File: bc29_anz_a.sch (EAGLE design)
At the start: 10 parts, among them IC2 MM74C945N, J1 2520-5

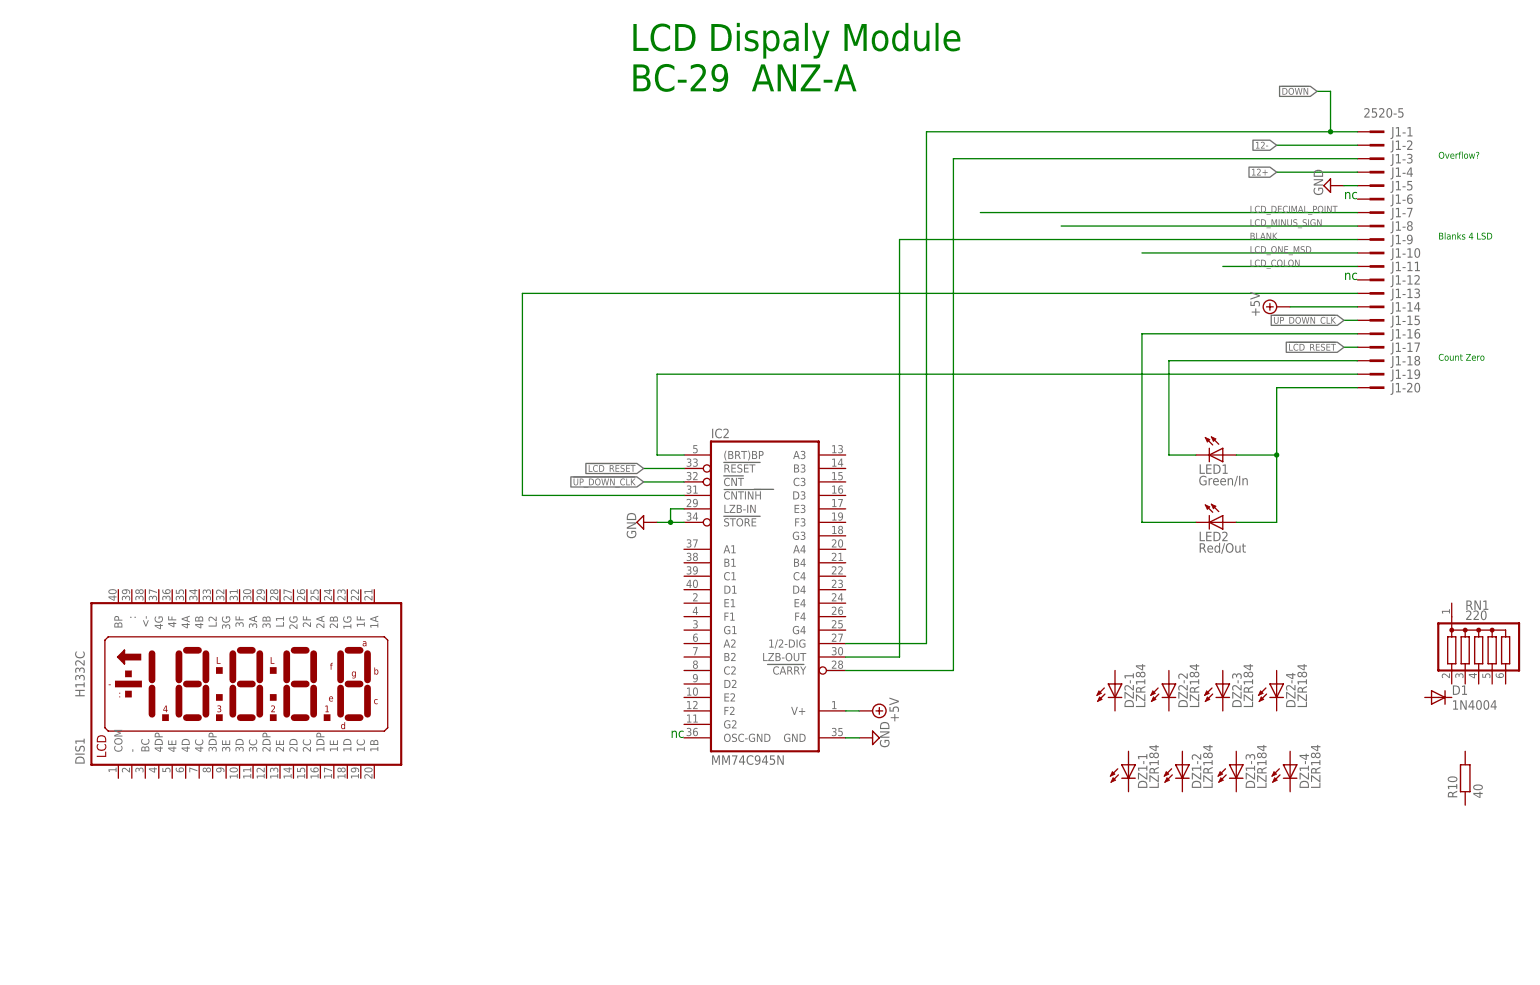
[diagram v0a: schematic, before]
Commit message: Incorperate display module knowldge
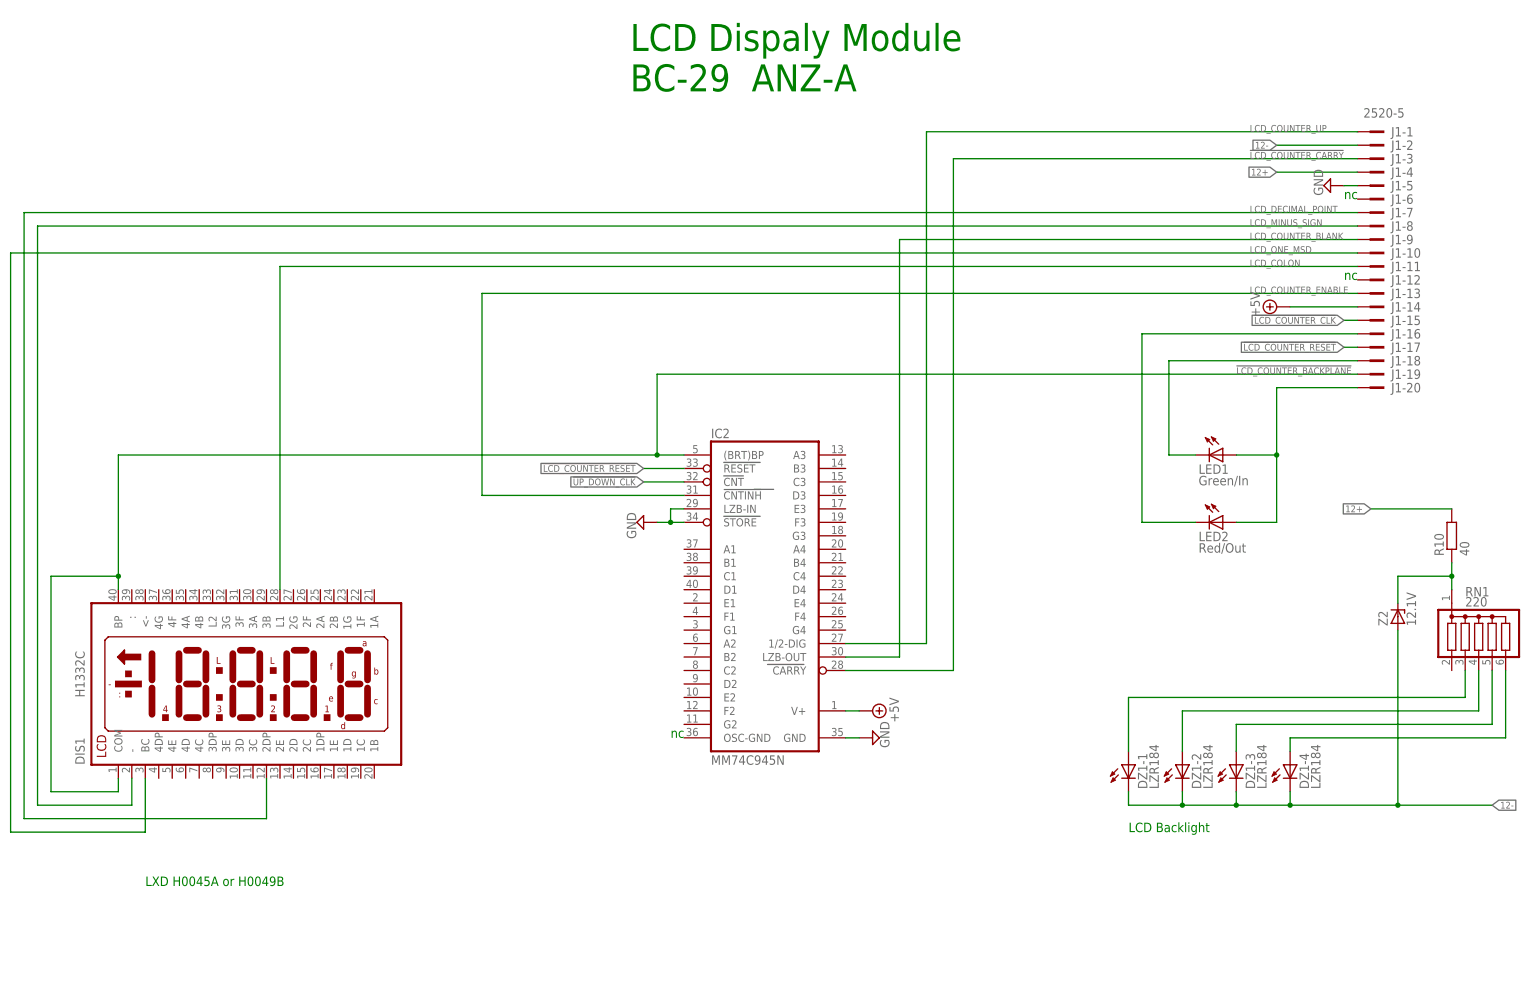
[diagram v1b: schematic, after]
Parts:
- removed D1: 1N4004, diode:1N4004
- removed DZ2: LZR184, led:LZR184
- added Z2: 12.1V, diode:ZENER-DIODESOD80C
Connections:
- net !CARRY renamed !LCD_COUNTER_CARRY
- net !DOWN renamed LCD_COUNTER_UP
- net !LCD_RESET renamed !LCD_COUNTER_RESET
- net BLANK renamed LCD_COUNTER_BLANK
- net ENABLE renamed LCD_COUNTER_ENABLE
- removed net LCD_45_HZ: IC2.(BRT)BP, J1-19.KL
- new net !LCD_COUNTER_BACKPLANE: DIS1.BP, DIS1.COM, IC2.(BRT)BP, J1-19.KL
- new net !LCD_COUNTER_CLK: J1-15.KL
- new net N$1: R10.1, RN1.1, Z2.C
- new net N$2: DZ1-4.A, RN1.6
- new net N$3: DZ1-3.A, RN1.5
- new net N$4: DZ1-2.A, RN1.4
- new net N$5: DZ1-1.A, RN1.3
- net !UP_DOWN_CLK: no longer J1-15.KL
- net 12+: now also R10.2
- net 12-: now also DZ1-1.C, DZ1-2.C, DZ1-3.C, DZ1-4.C, Z2.A
- net LCD_COLON: now also DIS1.L1
- net LCD_DECIMAL_POINT: now also DIS1.2DP
- net LCD_MINUS_SIGN: now also DIS1.-
- net LCD_ONE_MSD: now also DIS1.BC
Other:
- note added: "LCD Backlight"
- note added: "LXD H0045A or H0049B"
- note removed: "Blanks 4 LSD"
- note removed: "Count Zero"
- note removed: "Overflow?"
- moved on the sheet: R10, RN1

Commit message: Clean up net names
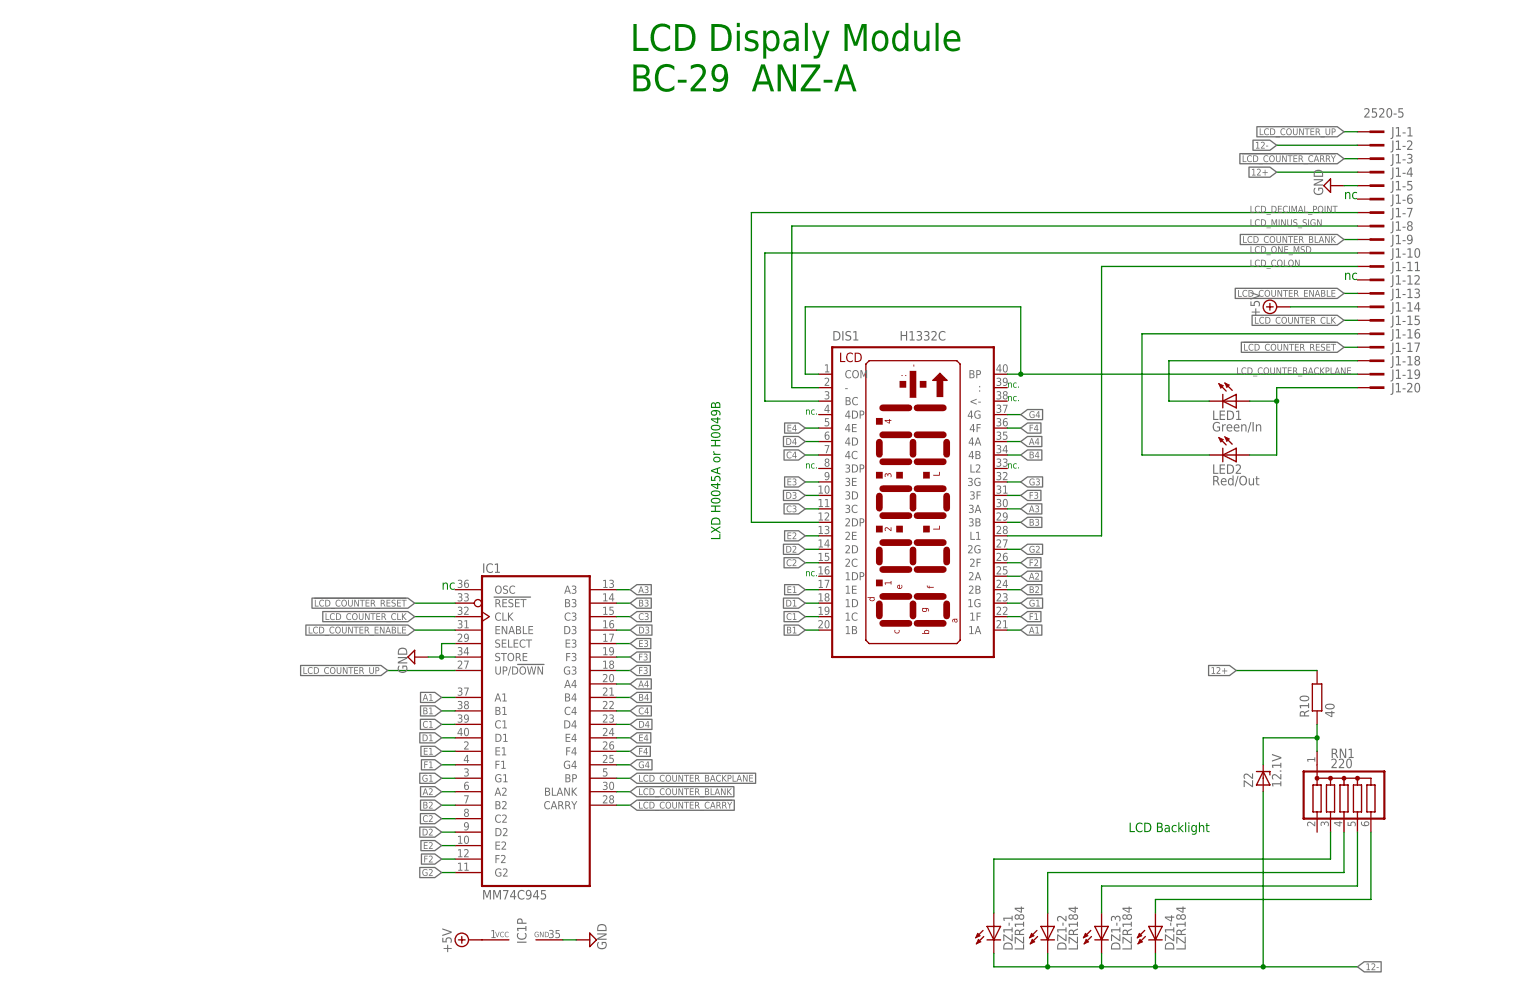
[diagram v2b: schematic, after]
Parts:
- removed IC2: MM74C945N, maxim:ICM7224PL
- added IC1: MM74C945, maxim:MM74C945
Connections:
- net N$1 renamed LED_V+
- net N$2 renamed BL3
- net N$3 renamed BL2
- net N$4 renamed BL1
- net N$5 renamed BL0
- removed net !LCD_COUNTER_BACKPLANE: DIS1.BP, DIS1.COM, IC2.(BRT)BP, J1-19.KL
- removed net !LCD_COUNTER_CLK: J1-15.KL
- removed net !UP_DOWN_CLK: IC2.CNT
- new net A1: DIS1.1A, IC1G$1.A1
- new net A2: DIS1.2A, IC1G$1.A2
- new net A3: DIS1.3A, IC1G$1.A3
- new net A4: DIS1.4A, IC1G$1.A4
- new net B1: DIS1.1B, IC1G$1.B1
- new net B2: DIS1.2B, IC1G$1.B2
- new net B3: DIS1.3B, IC1G$1.B3
- new net B4: DIS1.4B, IC1G$1.B4
- new net C1: DIS1.1C, IC1G$1.C1
- new net C2: DIS1.2C, IC1G$1.C2
- new net C3: DIS1.3C, IC1G$1.C3
- new net C4: DIS1.4C, IC1G$1.C4
- new net D1: DIS1.1D, IC1G$1.D1
- new net D2: DIS1.2D, IC1G$1.D2
- new net D3: DIS1.3D, IC1G$1.D3
- new net D4: DIS1.4D, IC1G$1.D4
- new net E1: DIS1.1E, IC1G$1.E1
- new net E2: DIS1.2E, IC1G$1.E2
- new net E3: DIS1.3E, IC1G$1.E3
- new net E4: DIS1.4E, IC1G$1.E4
- new net F1: DIS1.1F, IC1G$1.F1
- new net F2: DIS1.2F, IC1G$1.F2
- new net F3: DIS1.3F, IC1G$1.F3
- new net F4: DIS1.4F, IC1G$1.F4
- new net G1: DIS1.1G, IC1G$1.G1
- new net G2: DIS1.2G, IC1G$1.G2
- new net G3: DIS1.3G, IC1G$1.G3
- new net G4: DIS1.4G, IC1G$1.G4
- new net LCD_COUNTER_BACKPLANE: DIS1.BP, DIS1.COM, IC1G$1.BP, J1-19.KL
- new net LCD_COUNTER_CLK: IC1G$1.CLK, J1-15.KL
- net !LCD_COUNTER_CARRY: now also IC1G$1.CARRY; no longer IC2.CARRY
- net !LCD_COUNTER_RESET: now also IC1G$1.RESET; no longer IC2.RESET
- net +12V: now also IC1P.VCC; no longer IC2.V+
- net GND: now also IC1G$1.SELECT, IC1G$1.STORE, IC1P.GND; no longer IC2.GND, IC2.LZB-IN, IC2.STORE
- net LCD_COUNTER_BLANK: now also IC1G$1.BLANK; no longer IC2.LZB-OUT
- net LCD_COUNTER_ENABLE: now also IC1G$1.ENABLE; no longer IC2.!CNTINH
- net LCD_COUNTER_UP: now also IC1G$1.UP/DOWN; no longer IC2.1/2-DIG
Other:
- note added: "nc."
- moved on the sheet: DIS1, DZ1-1, DZ1-2, DZ1-3, DZ1-4, LED1, LED2, R10, RN1, Z2
